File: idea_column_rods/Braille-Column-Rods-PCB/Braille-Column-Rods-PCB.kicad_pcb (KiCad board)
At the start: 2 copper layers, 76 x 95 mm, 64 parts, among them J1 Conn_01x06, J10 Screw_Terminal_01x02, J2 Conn_01x06, J3 Conn_01x06, J4 Conn_01x06, J9 Conn_01x02, M1 Stepper_Motor_bipolar, M2 Stepper_Motor_bipolar, M3 Stepper_Motor_bipolar, M4 Stepper_Motor_bipolar, SW1 SW_Push, SW2 SW_Push, U1 DRV8847SPWR, U2 DRV8847SPWR, U3 DRV8847SPWR, U4 DRV8847SPWR, U9 RP2040-Zero

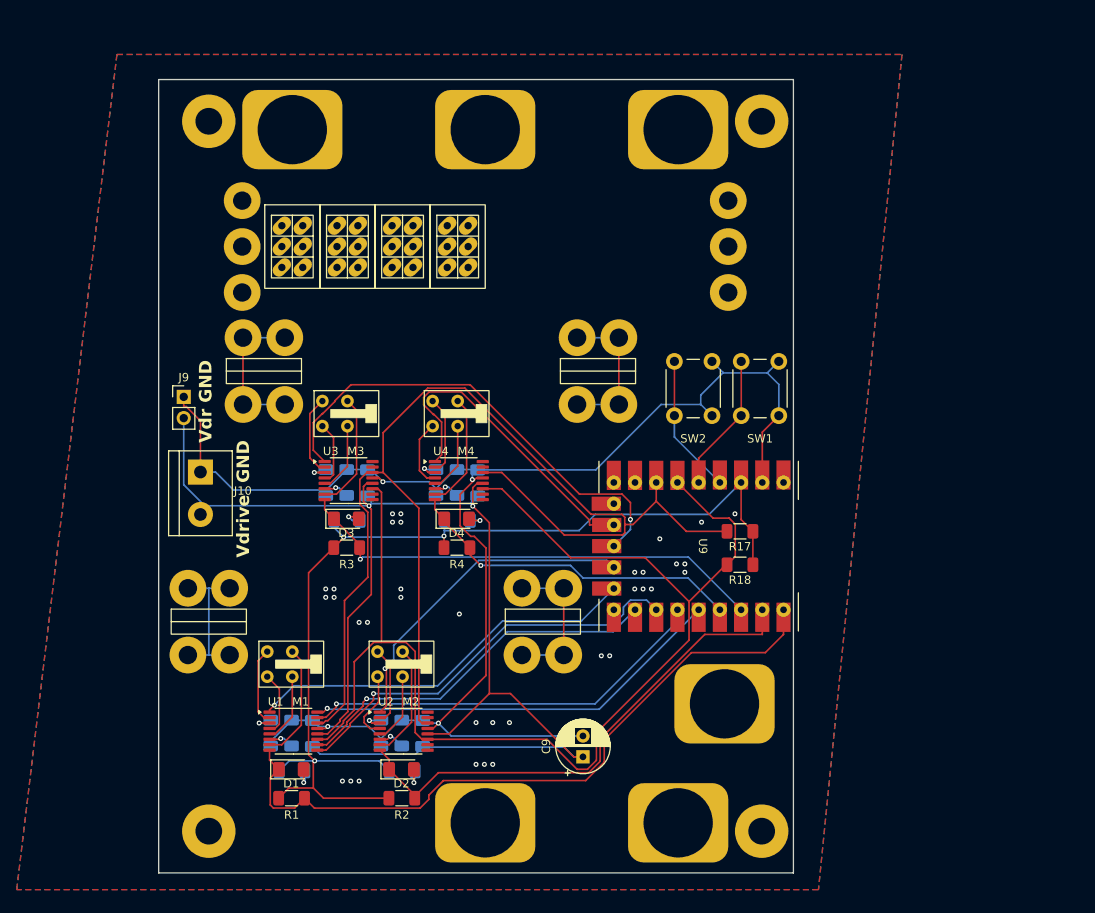
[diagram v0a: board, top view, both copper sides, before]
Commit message: Create PCB and CAD for Type 4 Rev 1 rod cams (#13)
* WIP: Rods PCB placement

* WIP: Place the housing and motor X

* WIP: Position everything

* WIP: Update tight placement of DC motor

* WIP: Layout and route the stepper driver

* WIP: Motor layout is good

* WIP: Manual routing and silkscreens

* Comments

* Big routing

* Clean up DRC (mostly footprints)

* Fix spacing issue on top

* Fix spacing issues on bottom

* Create render of 6mm motor, add to PCB

* WIP: Get cams good

* WIP: Reorder the cam bushing and hall sensor

* Finish and tag release

* Complete type 4 rev 1

* Create dc_motor_clamp cad
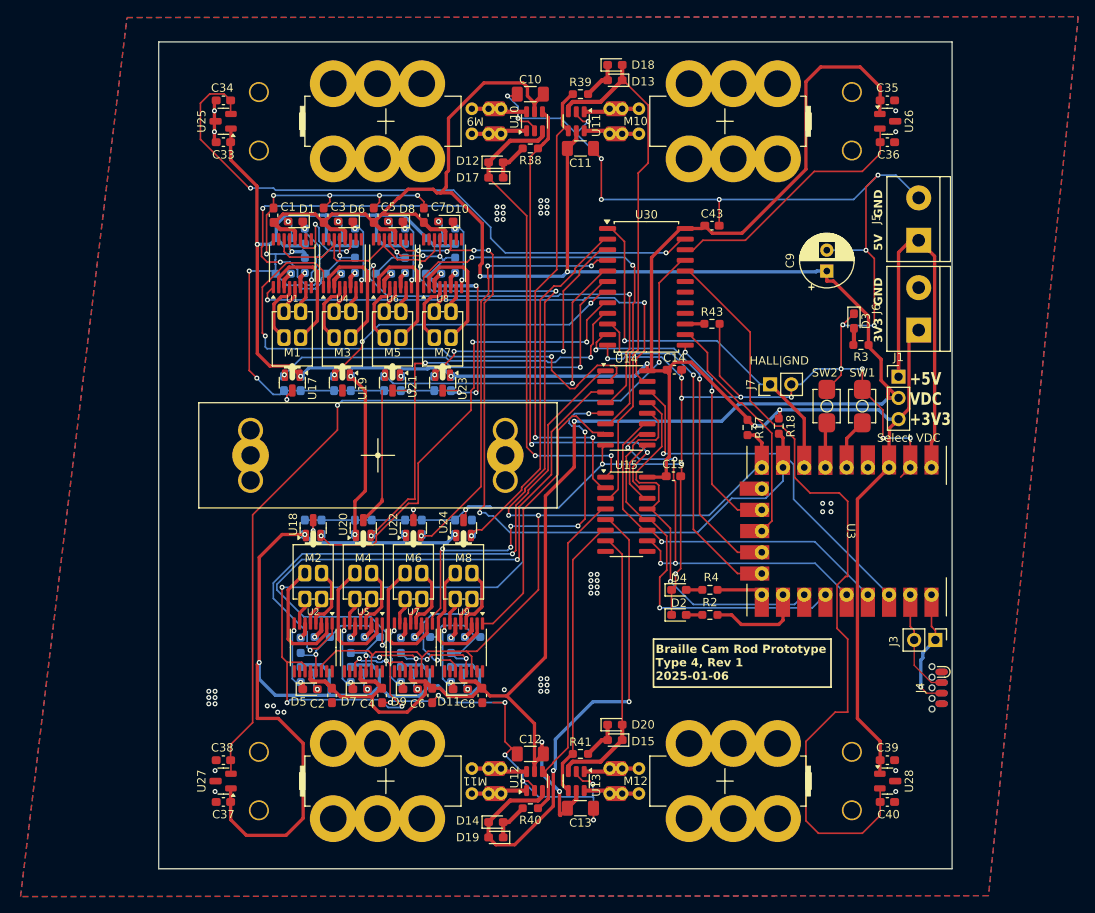
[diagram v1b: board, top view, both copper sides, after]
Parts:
- removed H10, H11, H12, H7, H8, H9: MountingHole_Pad, 00-lib-footprints:MountingHole_2.2mm_M2_Pad_NoSilk
- removed H13, H14, H15, H16: MountingHole_Pad, 00-lib-footprints:MountingHole_3.2mm_M3_Pad_NoSilk
- removed H17, H18, H19, H20: MountingHole_Pad, 00-lib-footprints:HorizMounting_4x_M2_and_M3_Middle
- removed H3, H4, H5, H6: MountingHole_Pad, 00-lib-footprints:MountingHole_8mm_Rect_NoSilk
- removed J10: Screw_Terminal_01x02, TerminalBlock:TerminalBlock_bornier-2_P5.08mm
- removed J2: Conn_01x06, 00-lib-footprints:Braille_Cell_Pogos_Solder_2.5mmIntra_6.6x10mmInter
- removed J9: Conn_01x02, Connector_PinHeader_2.54mm:PinHeader_1x02_P2.54mm_Vertical
- added C10: 10u, Capacitor_SMD:C_1206_3216Metric_Pad1.33x1.80mm_HandSolder, F.Cu at (128.5, 81.8)
- added C11: 10u, Capacitor_SMD:C_1206_3216Metric_Pad1.33x1.80mm_HandSolder, F.Cu at (134.5, 88.2)
- added C12: 10u, Capacitor_SMD:C_1206_3216Metric_Pad1.33x1.80mm_HandSolder, F.Cu at (128.5, 160.8)
- added C13: 10u, Capacitor_SMD:C_1206_3216Metric_Pad1.33x1.80mm_HandSolder, F.Cu at (134.5, 167.2)
- added C14: 100n, Capacitor_SMD:C_0603_1608Metric_Pad1.08x0.95mm_HandSolder, F.Cu at (145.8, 114.8)
- added C15: 100n, Capacitor_SMD:C_0603_1608Metric_Pad1.08x0.95mm_HandSolder, F.Cu at (145.6, 127.5)
- added C17: 100n, Capacitor_SMD:C_0603_1608Metric_Pad1.08x0.95mm_HandSolder, B.Cu at (101.0, 116.4)
- added C18: 100n, Capacitor_SMD:C_0603_1608Metric_Pad1.08x0.95mm_HandSolder, B.Cu at (101.5, 133.6)
- added C19: 100n, Capacitor_SMD:C_0603_1608Metric_Pad1.08x0.95mm_HandSolder, B.Cu at (107.0, 116.4)
- added C20: 100n, Capacitor_SMD:C_0603_1608Metric_Pad1.08x0.95mm_HandSolder, B.Cu at (107.5, 133.6)
- added C21: 100n, Capacitor_SMD:C_0603_1608Metric_Pad1.08x0.95mm_HandSolder, B.Cu at (113.0, 116.4)
- added C22: 100n, Capacitor_SMD:C_0603_1608Metric_Pad1.08x0.95mm_HandSolder, B.Cu at (113.5, 133.6)
- added C23: 100n, Capacitor_SMD:C_0603_1608Metric_Pad1.08x0.95mm_HandSolder, B.Cu at (119.0, 116.4)
- added C24: 100n, Capacitor_SMD:C_0603_1608Metric_Pad1.08x0.95mm_HandSolder, B.Cu at (119.5, 133.6)
- added C25: 4.7n, Capacitor_SMD:C_0603_1608Metric_Pad1.08x0.95mm_HandSolder, B.Cu at (99.0, 116.4)
- added C26: 4.7n, Capacitor_SMD:C_0603_1608Metric_Pad1.08x0.95mm_HandSolder, B.Cu at (103.5, 133.6)
- added C27: 4.7n, Capacitor_SMD:C_0603_1608Metric_Pad1.08x0.95mm_HandSolder, B.Cu at (105.0, 116.4)
- added C28: 4.7n, Capacitor_SMD:C_0603_1608Metric_Pad1.08x0.95mm_HandSolder, B.Cu at (109.5, 133.6)
- added C29: 4.7n, Capacitor_SMD:C_0603_1608Metric_Pad1.08x0.95mm_HandSolder, B.Cu at (111.0, 116.4)
- added C30: 4.7n, Capacitor_SMD:C_0603_1608Metric_Pad1.08x0.95mm_HandSolder, B.Cu at (115.5, 133.6)
- added C31: 4.7n, Capacitor_SMD:C_0603_1608Metric_Pad1.08x0.95mm_HandSolder, B.Cu at (117.0, 116.4)
- added C32: 4.7n, Capacitor_SMD:C_0603_1608Metric_Pad1.08x0.95mm_HandSolder, B.Cu at (121.5, 133.6)
- added C33: 100n, Capacitor_SMD:C_0603_1608Metric_Pad1.08x0.95mm_HandSolder, F.Cu at (91.8, 87.5)
- added C34: 4.7n, Capacitor_SMD:C_0603_1608Metric_Pad1.08x0.95mm_HandSolder, F.Cu at (91.8, 82.5)
- added C35: 100n, Capacitor_SMD:C_0603_1608Metric_Pad1.08x0.95mm_HandSolder, F.Cu at (171.2, 82.5)
- added C36: 4.7n, Capacitor_SMD:C_0603_1608Metric_Pad1.08x0.95mm_HandSolder, F.Cu at (171.2, 87.5)
- added C37: 100n, Capacitor_SMD:C_0603_1608Metric_Pad1.08x0.95mm_HandSolder, F.Cu at (91.8, 166.5)
- added C38: 4.7n, Capacitor_SMD:C_0603_1608Metric_Pad1.08x0.95mm_HandSolder, F.Cu at (91.8, 161.5)
- added C39: 100n, Capacitor_SMD:C_0603_1608Metric_Pad1.08x0.95mm_HandSolder, F.Cu at (171.2, 161.5)
- added C40: 4.7n, Capacitor_SMD:C_0603_1608Metric_Pad1.08x0.95mm_HandSolder, F.Cu at (171.2, 166.5)
- added C43: 100n, Capacitor_SMD:C_0603_1608Metric_Pad1.08x0.95mm_HandSolder, F.Cu at (150.2, 97.5)
- added C5: 100n, Capacitor_SMD:C_0603_1608Metric_Pad1.08x0.95mm_HandSolder, F.Cu at (109.8, 96.2)
- added C6: 100n, Capacitor_SMD:C_0603_1608Metric_Pad1.08x0.95mm_HandSolder, F.Cu at (116.8, 153.8)
- added C7: 100n, Capacitor_SMD:C_0603_1608Metric_Pad1.08x0.95mm_HandSolder, F.Cu at (115.8, 96.2)
- added C8: 100n, Capacitor_SMD:C_0603_1608Metric_Pad1.08x0.95mm_HandSolder, F.Cu at (122.8, 153.8)
- added D10: LED, LED_SMD:LED_0603_1608Metric_Pad1.05x0.95mm_HandSolder, F.Cu at (118.4, 97.0)
- added D11: LED, LED_SMD:LED_0603_1608Metric_Pad1.05x0.95mm_HandSolder, F.Cu at (120.1, 153.0)
- added D12: LED, LED_SMD:LED_0603_1608Metric_Pad1.05x0.95mm_HandSolder, F.Cu at (124.4, 89.9)
- added D13: LED, LED_SMD:LED_0603_1608Metric_Pad1.05x0.95mm_HandSolder, F.Cu at (138.6, 80.1)
- added D14: LED, LED_SMD:LED_0603_1608Metric_Pad1.05x0.95mm_HandSolder, F.Cu at (124.4, 168.9)
- added D15: LED, LED_SMD:LED_0603_1608Metric_Pad1.05x0.95mm_HandSolder, F.Cu at (138.6, 159.1)
- added D17: LED, LED_SMD:LED_0603_1608Metric_Pad1.05x0.95mm_HandSolder, F.Cu at (124.4, 91.8)
- added D18: LED, LED_SMD:LED_0603_1608Metric_Pad1.05x0.95mm_HandSolder, F.Cu at (138.6, 78.3)
- added D19: LED, LED_SMD:LED_0603_1608Metric_Pad1.05x0.95mm_HandSolder, F.Cu at (124.4, 170.8)
- added D20: LED, LED_SMD:LED_0603_1608Metric_Pad1.05x0.95mm_HandSolder, F.Cu at (138.6, 157.3)
- added D5: LED, LED_SMD:LED_0603_1608Metric_Pad1.05x0.95mm_HandSolder, F.Cu at (102.1, 153.0)
- added D6: LED, LED_SMD:LED_0603_1608Metric_Pad1.05x0.95mm_HandSolder, F.Cu at (106.4, 97.0)
- added D7: LED, LED_SMD:LED_0603_1608Metric_Pad1.05x0.95mm_HandSolder, F.Cu at (108.1, 153.0)
- added D8: LED, LED_SMD:LED_0603_1608Metric_Pad1.05x0.95mm_HandSolder, F.Cu at (112.4, 97.0)
- added D9: LED, LED_SMD:LED_0603_1608Metric_Pad1.05x0.95mm_HandSolder, F.Cu at (114.1, 153.0)
- added J5: Screw_Terminal_01x02, TerminalBlock:TerminalBlock_bornier-2_P5.08mm, F.Cu at (175.0, 99.2)
- added J6: Screw_Terminal_01x02, TerminalBlock:TerminalBlock_bornier-2_P5.08mm, F.Cu at (175.0, 110.0)
- added J7: Conn_01x02, Connector_PinHeader_2.54mm:PinHeader_1x02_P2.54mm_Vertical, F.Cu at (157.2, 116.5)
- added M10: Motor_DC_With_MP, 00-lib-footprints:DC_Motor_6mm_OD_with_3_Stage_Gearbox, F.Cu at (162.6, 85.0)
- added M11: Motor_DC_With_MP, 00-lib-footprints:DC_Motor_6mm_OD_with_3_Stage_Gearbox, F.Cu at (100.4, 164.0)
- added M12: Motor_DC_With_MP, 00-lib-footprints:DC_Motor_6mm_OD_with_3_Stage_Gearbox, F.Cu at (162.6, 164.0)
- added M5: Stepper_Motor_bipolar, 00-lib-footprints:MicroStepper_4.7_OD, F.Cu at (112.0, 114.7)
- added M6: Stepper_Motor_bipolar, 00-lib-footprints:MicroStepper_4.7_OD, F.Cu at (114.5, 135.3)
- added M7: Stepper_Motor_bipolar, 00-lib-footprints:MicroStepper_4.7_OD, F.Cu at (118.0, 114.7)
- added M8: Stepper_Motor_bipolar, 00-lib-footprints:MicroStepper_4.7_OD, F.Cu at (120.5, 135.3)
- added M9: Motor_DC_With_MP, 00-lib-footprints:DC_Motor_6mm_OD_with_3_Stage_Gearbox, F.Cu at (100.4, 85.0)
- added R13: 2k1, Resistor_SMD:R_0603_1608Metric_Pad0.98x0.95mm_HandSolder, B.Cu at (105.0, 99.0)
- added R14: 330m, Resistor_SMD:R_0603_1608Metric_Pad0.98x0.95mm_HandSolder, B.Cu at (107.5, 102.2)
- added R15: 330m, Resistor_SMD:R_0603_1608Metric_Pad0.98x0.95mm_HandSolder, B.Cu at (104.9, 103.2)
- added R16: 5k1, Resistor_SMD:R_0603_1608Metric_Pad0.98x0.95mm_HandSolder, B.Cu at (107.0, 151.2)
- added R23: 2k1, Resistor_SMD:R_0603_1608Metric_Pad0.98x0.95mm_HandSolder, B.Cu at (111.0, 99.0)
- added R24: 330m, Resistor_SMD:R_0603_1608Metric_Pad0.98x0.95mm_HandSolder, B.Cu at (113.5, 102.2)
- added R25: 330m, Resistor_SMD:R_0603_1608Metric_Pad0.98x0.95mm_HandSolder, B.Cu at (110.9, 103.2)
- added R26: 5k1, Resistor_SMD:R_0603_1608Metric_Pad0.98x0.95mm_HandSolder, B.Cu at (113.0, 151.2)
- added R31: 2k1, Resistor_SMD:R_0603_1608Metric_Pad0.98x0.95mm_HandSolder, B.Cu at (117.0, 99.0)
- added R32: 330m, Resistor_SMD:R_0603_1608Metric_Pad0.98x0.95mm_HandSolder, B.Cu at (119.5, 102.2)
- added R33: 330m, Resistor_SMD:R_0603_1608Metric_Pad0.98x0.95mm_HandSolder, B.Cu at (116.9, 103.2)
- added R34: 5k1, Resistor_SMD:R_0603_1608Metric_Pad0.98x0.95mm_HandSolder, B.Cu at (119.0, 151.2)
- added R35: 2k1, Resistor_SMD:R_0603_1608Metric_Pad0.98x0.95mm_HandSolder, B.Cu at (121.5, 151.0)
- added R36: 330m, Resistor_SMD:R_0603_1608Metric_Pad0.98x0.95mm_HandSolder, B.Cu at (119.0, 147.8)
- added R37: 330m, Resistor_SMD:R_0603_1608Metric_Pad0.98x0.95mm_HandSolder, B.Cu at (121.6, 146.8)
- added R38: 5k1, Resistor_SMD:R_0603_1608Metric_Pad0.98x0.95mm_HandSolder, F.Cu at (128.5, 88.2)
- added R39: 5k1, Resistor_SMD:R_0603_1608Metric_Pad0.98x0.95mm_HandSolder, F.Cu at (134.5, 81.8)
- added R40: 5k1, Resistor_SMD:R_0603_1608Metric_Pad0.98x0.95mm_HandSolder, F.Cu at (128.5, 167.2)
- added R41: 5k1, Resistor_SMD:R_0603_1608Metric_Pad0.98x0.95mm_HandSolder, F.Cu at (134.5, 160.8)
- added R43: 5k1, Resistor_SMD:R_0603_1608Metric_Pad0.98x0.95mm_HandSolder, F.Cu at (150.2, 109.2)
- added R5: 2k1, Resistor_SMD:R_0603_1608Metric_Pad0.98x0.95mm_HandSolder, B.Cu at (99.0, 99.0)
- added R6: 330m, Resistor_SMD:R_0603_1608Metric_Pad0.98x0.95mm_HandSolder, B.Cu at (101.5, 102.2)
- added R7: 330m, Resistor_SMD:R_0603_1608Metric_Pad0.98x0.95mm_HandSolder, B.Cu at (98.9, 103.2)
- added R8: 5k1, Resistor_SMD:R_0603_1608Metric_Pad0.98x0.95mm_HandSolder, B.Cu at (101.0, 151.2)
- added U10: AD116, Package_TO_SOT_SMD:SOT-23-6, F.Cu at (129.0, 85.0)
- added U11: AD116, Package_TO_SOT_SMD:SOT-23-6, F.Cu at (134.0, 85.0)
- added U12: AD116, Package_TO_SOT_SMD:SOT-23-6, F.Cu at (129.0, 164.0)
- added U13: AD116, Package_TO_SOT_SMD:SOT-23-6, F.Cu at (134.0, 164.0)
- added U14: 74HC595, Package_SO:SOP-16_3.9x9.9mm_P1.27mm, F.Cu at (140.0, 119.3)
- added U15: 74HC595, Package_SO:SOP-16_3.9x9.9mm_P1.27mm, F.Cu at (140.0, 132.1)
- added U17: MT910xET, 00-lib-footprints:SOT-23-Hall, F.Cu at (100.0, 116.3)
- added U18: MT910xET, 00-lib-footprints:SOT-23-Hall, F.Cu at (102.5, 133.7)
- added U19: MT910xET, 00-lib-footprints:SOT-23-Hall, F.Cu at (106.0, 116.3)
- added U20: MT910xET, 00-lib-footprints:SOT-23-Hall, F.Cu at (108.5, 133.7)
- added U21: MT910xET, 00-lib-footprints:SOT-23-Hall, F.Cu at (112.0, 116.3)
- added U22: MT910xET, 00-lib-footprints:SOT-23-Hall, F.Cu at (114.5, 133.7)
- added U23: MT910xET, 00-lib-footprints:SOT-23-Hall, F.Cu at (118.0, 116.3)
- added U24: MT910xET, 00-lib-footprints:SOT-23-Hall, F.Cu at (120.5, 133.7)
- added U25: MT910xET, 00-lib-footprints:SOT-23-Hall, F.Cu at (91.8, 85.0)
- added U26: MT910xET, 00-lib-footprints:SOT-23-Hall, F.Cu at (171.2, 85.0)
- added U27: MT910xET, 00-lib-footprints:SOT-23-Hall, F.Cu at (91.8, 164.0)
- added U28: MT910xET, 00-lib-footprints:SOT-23-Hall, F.Cu at (171.2, 164.0)
- added U30: CD74HC4067M, Package_SO:SOIC-24W_7.5x15.4mm_P1.27mm, F.Cu at (142.4, 104.8)
- added U5: DRV8847SPWR, Package_SO:TSSOP-16_4.4x5mm_P0.65mm, F.Cu at (108.5, 148.0)
- added U6: DRV8847SPWR, Package_SO:TSSOP-16_4.4x5mm_P0.65mm, F.Cu at (112.0, 102.0)
- added U7: DRV8847SPWR, Package_SO:TSSOP-16_4.4x5mm_P0.65mm, F.Cu at (114.5, 148.0)
- added U8: DRV8847SPWR, Package_SO:TSSOP-16_4.4x5mm_P0.65mm, F.Cu at (118.0, 102.0)
- C1, C2, C3, C4: footprint Capacitor_SMD:C_1206_3216Metric_Pad1.33x1.80mm_HandSolder -> Capacitor_SMD:C_0603_1608Metric_Pad1.08x0.95mm_HandSolder; moved to F.Cu
- D1, D2, D3, D4: footprint LED_SMD:LED_1206_3216Metric_Pad1.42x1.75mm_HandSolder -> LED_SMD:LED_0603_1608Metric_Pad1.05x0.95mm_HandSolder
- H1, H2: footprint 00-lib-footprints:MountingHole_8mm_Rect_NoSilk -> 00-lib-footprints:Braille_Block_MountingHoles_M2_3x
- J1: value Conn_01x06 -> Conn_01x03; footprint 00-lib-footprints:Braille_Cell_Pogos_Solder_2.5mmIntra_6.6x10mmInter -> Connector_PinHeader_2.54mm:PinHeader_1x03_P2.54mm_Vertical
- J3: value Conn_01x06 -> Conn_01x02; footprint 00-lib-footprints:Braille_Cell_Pogos_Solder_2.5mmIntra_6.6x10mmInter -> Connector_PinHeader_2.54mm:PinHeader_1x02_P2.54mm_Vertical
- J4: value Conn_01x06 -> Conn_01x08; footprint 00-lib-footprints:Braille_Cell_Pogos_Solder_2.5mmIntra_6.6x10mmInter -> 00-lib-footprints:SOICbite_clipProgSmall
- M1, M2, M3, M4: footprint 00-lib-footprints:MicroStepper_8mm-2mmGear -> 00-lib-footprints:MicroStepper_4.7_OD
- R1: footprint Resistor_SMD:R_1206_3216Metric_Pad1.30x1.75mm_HandSolder -> Resistor_SMD:R_0603_1608Metric_Pad0.98x0.95mm_HandSolder; moved to B.Cu
- R10, R11: value 2k1 -> 330m; footprint Resistor_SMD:R_1206_3216Metric_Pad1.30x1.75mm_HandSolder -> Resistor_SMD:R_0603_1608Metric_Pad0.98x0.95mm_HandSolder
- R12: value 2k1 -> 5k1; footprint Resistor_SMD:R_1206_3216Metric_Pad1.30x1.75mm_HandSolder -> Resistor_SMD:R_0603_1608Metric_Pad0.98x0.95mm_HandSolder
- R17, R18, R2, R20, R21, R28, R29, R3, R4, R9: footprint Resistor_SMD:R_1206_3216Metric_Pad1.30x1.75mm_HandSolder -> Resistor_SMD:R_0603_1608Metric_Pad0.98x0.95mm_HandSolder
- R19, R27: value 330m -> 2k1; footprint Resistor_SMD:R_1206_3216Metric_Pad1.30x1.75mm_HandSolder -> Resistor_SMD:R_0603_1608Metric_Pad0.98x0.95mm_HandSolder
- R22, R30: value 330m -> 5k1; footprint Resistor_SMD:R_1206_3216Metric_Pad1.30x1.75mm_HandSolder -> Resistor_SMD:R_0603_1608Metric_Pad0.98x0.95mm_HandSolder
- SW1, SW2: footprint Button_Switch_THT:SW_PUSH_6mm -> 00-lib-footprints:PushButtonSMD_2.93x3.9
- U3: value DRV8847SPWR -> RP2040-Zero; footprint Package_SO:TSSOP-16_4.4x5mm_P0.65mm -> 00-lib-footprints:RP2040 Zero
- U9: value RP2040-Zero -> DRV8847SPWR; footprint 00-lib-footprints:RP2040 Zero -> Package_SO:TSSOP-16_4.4x5mm_P0.65mm
- moved J3 84.7 mm to (177.0, 147.1), turned to -90 degrees
- moved J4 79.0 mm to (178.5, 152.8), turned to 90 degrees
- moved J1 74.2 mm to (172.6, 115.6)
- moved R1 67.3 mm to (101.5, 98.8), turned to 90 degrees
- moved R3 66.2 mm to (168.1, 111.8), turned to 180 degrees
- moved D1 65.6 mm to (100.4, 97.0), turned to 180 degrees
- moved D3 65.2 mm to (167.2, 108.9), turned to -90 degrees
- moved C9 65.1 mm to (164.0, 102.9)
- moved C1 62.2 mm to (97.8, 96.2)
- moved U1 56.0 mm to (100.0, 102.0), turned to 90 degrees
- moved H1 48.1 mm to (95.0, 125.0)
- moved U3 47.0 mm to (153.5, 123.9), turned to -90 degrees
- moved H2 44.1 mm to (125.5, 125.0)
- moved R2 42.9 mm to (150.0, 144.1), turned to 180 degrees
- moved D2 38.0 mm to (146.3, 144.1)
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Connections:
- C1 pad 1: Vdrive -> VDC
- C2 pad 1: Vdrive -> VDC
- C3 pad 1: Vdrive -> VDC
- C4 pad 1: Vdrive -> VDC
- C9 pad 1: Vdrive -> VDC
- D1 pad 1: /Braille_Cell/~{FAULT} -> /Motor_Control/Braille_Cell_Column/~{FAULT}
- D2 pad 1: /Braille_Cell1/~{FAULT} -> GND
- D3 pad 1: /Braille_Cell2/~{FAULT} -> GND
- D4 pad 1: /Braille_Cell3/~{FAULT} -> GND
- J1 pad 1: unconnected-(J1-Pin_1-Pad1) -> +5V
- J1 pad 2: unconnected-(J1-Pin_2-Pad2) -> VDC
- J1 pad 3: unconnected-(J1-Pin_3-Pad3) -> +3V3
- J3 pad 1: unconnected-(J3-Pin_1-Pad1) -> /Microcontroller/UART0_TX
- J3 pad 2: unconnected-(J3-Pin_2-Pad2) -> /Microcontroller/UART0_RX
- J4 pad 2: unconnected-(J4-Pin_2-Pad2) -> /Microcontroller/UART0_RX
- J4 pad 3: unconnected-(J4-Pin_3-Pad3) -> /Microcontroller/UART0_TX
- J4 pad 4: unconnected-(J4-Pin_4-Pad4) -> GND
- M3 pad 1: Net-(U3-OUT1) -> Net-(U4-OUT1)
- M3 pad 3: Net-(U3-OUT3) -> Net-(U4-OUT3)
- M3 pad 4: Net-(U3-OUT4) -> Net-(U4-OUT4)
- M4 pad 1: Net-(U4-OUT1) -> Net-(U5-OUT1)
- M4 pad 3: Net-(U4-OUT3) -> Net-(U5-OUT3)
- M4 pad 4: Net-(U4-OUT4) -> Net-(U5-OUT4)
- R1 pad 2: /Braille_Cell/~{FAULT} -> /Motor_Control/Braille_Cell_Column/~{FAULT}
- R10 pad 1: +3V3 -> Net-(U2-ISEN34)
- R10 pad 2: Net-(D2-A) -> GND
- R11 pad 1: +3V3 -> Net-(U2-ISEN12)
- R11 pad 2: Net-(D3-A) -> GND
- R12 pad 2: Net-(D4-A) -> /Motor_Control/Braille_Cell_Column2/~{FAULT}
- R19 pad 1: Net-(U1-ISEN34) -> +3V3
- R19 pad 2: GND -> Net-(D7-A)
- R2 pad 1: +3V3 -> /Microcontroller/GP_LED_0
- R2 pad 2: /Braille_Cell1/~{FAULT} -> Net-(D2-A)
- R20 pad 1: Net-(U2-ISEN34) -> Net-(U5-ISEN34)
- R21 pad 1: Net-(U3-ISEN34) -> Net-(U5-ISEN12)
- R22 pad 1: Net-(U4-ISEN34) -> +3V3
- R22 pad 2: GND -> /Motor_Control/Braille_Cell_Column4/~{FAULT}
- R27 pad 1: Net-(U1-ISEN12) -> +3V3
- R27 pad 2: GND -> Net-(D9-A)
- R28 pad 1: Net-(U2-ISEN12) -> Net-(U7-ISEN34)
- R29 pad 1: Net-(U3-ISEN12) -> Net-(U7-ISEN12)
- R3 pad 1: +3V3 -> VDC
- R3 pad 2: /Braille_Cell2/~{FAULT} -> Net-(D3-A)
- R30 pad 1: Net-(U4-ISEN12) -> +3V3
- R30 pad 2: GND -> /Motor_Control/Braille_Cell_Column6/~{FAULT}
- R4 pad 1: +3V3 -> /Microcontroller/GP_LED_1
- R4 pad 2: /Braille_Cell3/~{FAULT} -> Net-(D4-A)
- R9 pad 2: Net-(D1-A) -> Net-(D5-A)
- SW1 pad 2: Net-(U9-GP28) -> /Microcontroller/SW_1
- SW2 pad 2: Net-(U9-GP29) -> /Microcontroller/SW_2
- U1 pad 1: /Braille_Cell/~{SLEEP} -> /Motor_Control/Braille_Cell_Column/~{SLEEP}
- U1 pad 10: /Braille_Cell/IN4 -> unconnected-(U1-IN4-Pad10)
- U1 pad 12: Vdrive -> VDC
- U1 pad 15: /Braille_Cell/IN2 -> unconnected-(U1-IN2-Pad15)
- U1 pad 16: /Braille_Cell/IN1 -> unconnected-(U1-IN1-Pad16)
- U1 pad 8: /Braille_Cell/~{FAULT} -> /Motor_Control/Braille_Cell_Column/~{FAULT}
- U1 pad 9: /Braille_Cell/IN3 -> unconnected-(U1-IN3-Pad9)
- U2 pad 1: /Braille_Cell1/~{SLEEP} -> /Motor_Control/Braille_Cell_Column1/~{SLEEP}
- U2 pad 10: /Braille_Cell1/IN4 -> unconnected-(U2-IN4-Pad10)
- U2 pad 12: Vdrive -> VDC
- U2 pad 15: /Braille_Cell1/IN2 -> unconnected-(U2-IN2-Pad15)
- U2 pad 16: /Braille_Cell1/IN1 -> unconnected-(U2-IN1-Pad16)
- U2 pad 8: /Braille_Cell1/~{FAULT} -> /Motor_Control/Braille_Cell_Column1/~{FAULT}
- U2 pad 9: /Braille_Cell1/IN3 -> unconnected-(U2-IN3-Pad9)
- U3 pad 1: /Braille_Cell2/~{SLEEP} -> +5V
- U3 pad 10: /Braille_Cell2/IN4 -> /Microcontroller/UART0_TX
- U3 pad 11: I2C_SCL -> /Microcontroller/UART0_RX
- U3 pad 12: Vdrive -> /Microcontroller/SHIFT_SER_IN
- U3 pad 13: GND -> /Microcontroller/SHIFT_SRCK
- U3 pad 14: I2C_SDA -> /Microcontroller/~{SHIFT_SRCLR}
- U3 pad 15: /Braille_Cell2/IN2 -> /Microcontroller/SHIFT_RCLK
- U3 pad 16: /Braille_Cell2/IN1 -> /Microcontroller/~{SHIFT_OE}
- U3 pad 2: Net-(U3-OUT1) -> GND
- U3 pad 3: Net-(U3-ISEN12) -> +3V3
- U3 pad 4: Net-(M3--) -> unconnected-(U3-GP29-Pad4)
- U3 pad 5: Net-(U3-OUT4) -> /Microcontroller/SW_1
- U3 pad 6: Net-(U3-ISEN34) -> /Microcontroller/SW_2
- U3 pad 7: Net-(U3-OUT3) -> /Microcontroller/HALL_ANALOG
- U3 pad 8: /Braille_Cell2/~{FAULT} -> I2C_SCL
- U3 pad 9: /Braille_Cell2/IN3 -> I2C_SDA
- U4 pad 1: /Braille_Cell3/~{SLEEP} -> /Motor_Control/Braille_Cell_Column2/~{SLEEP}
- U4 pad 10: /Braille_Cell3/IN4 -> unconnected-(U4-IN4-Pad10)
- U4 pad 12: Vdrive -> VDC
- U4 pad 15: /Braille_Cell3/IN2 -> unconnected-(U4-IN2-Pad15)
- U4 pad 16: /Braille_Cell3/IN1 -> unconnected-(U4-IN1-Pad16)
- U4 pad 4: Net-(M4--) -> Net-(M3--)
- U4 pad 8: /Braille_Cell3/~{FAULT} -> /Motor_Control/Braille_Cell_Column2/~{FAULT}
- U4 pad 9: /Braille_Cell3/IN3 -> unconnected-(U4-IN3-Pad9)
- U9 pad 1: +5V -> /Motor_Control/Braille_Cell_Column7/~{SLEEP}
- U9 pad 10: /Braille_Cell/~{FAULT} -> unconnected-(U9-IN4-Pad10)
- U9 pad 11: /Braille_Cell1/~{FAULT} -> I2C_SCL
- U9 pad 12: /Braille_Cell2/~{FAULT} -> VDC
- U9 pad 13: /Braille_Cell3/~{FAULT} -> GND
- U9 pad 14: /Braille_Cell/IN1 -> I2C_SDA
- U9 pad 15: /Braille_Cell/IN2 -> unconnected-(U9-IN2-Pad15)
- U9 pad 16: /Braille_Cell/IN3 -> unconnected-(U9-IN1-Pad16)
- U9 pad 2: GND -> Net-(U9-OUT1)
- U9 pad 3: +3V3 -> Net-(U9-ISEN12)
- U9 pad 4: Net-(U9-GP29) -> Net-(M8--)
- U9 pad 5: Net-(U9-GP28) -> Net-(U9-OUT4)
- U9 pad 6: I2C_SCL -> Net-(U9-ISEN34)
- U9 pad 7: I2C_SDA -> Net-(U9-OUT3)
- U9 pad 8: unconnected-(U9-GP15-Pad8)_1 -> /Motor_Control/Braille_Cell_Column7/~{FAULT}
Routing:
- net GND: track 192.0 -> 530.2 mm, vias 39 -> 104
- net +3V3: track 127.6 -> 448.9 mm, vias 3 -> 13
- net VDC: track 0.00 -> 314.4 mm, vias 0 -> 5
- net Vdrive: track 166.6 -> 0.00 mm, vias 2 -> 0
- net /Motor_Control/HALL_10: track 0.00 -> 103.8 mm, vias 0 -> 2
- net I2C_SCL: track 148.8 -> 251.8 mm, vias 0 -> 15
- net /Motor_Control/HALL_11: track 0.00 -> 94.4 mm
- net /Braille_Cell/~{FAULT}: track 83.4 -> 0.00 mm
- net /Motor_Control/Braille_Cell_Column3/~{SLEEP}: track 0.00 -> 75.7 mm, vias 0 -> 2
- net /Motor_Control/HALL_8: track 0.00 -> 75.5 mm, vias 0 -> 2
- net /Motor_Control/Braille_Cell_Column1/~{SLEEP}: track 0.00 -> 71.4 mm, vias 0 -> 2
- net /Motor_Control/Braille_Cell_Column2/~{SLEEP}: track 0.00 -> 67.0 mm, vias 0 -> 2
- net /Motor_Control/Corner_DC_Motor1/IN_B: track 0.00 -> 64.0 mm
- net /Motor_Control/Corner_DC_Motor/IN_A: track 0.00 -> 62.6 mm, vias 0 -> 2
- net /Motor_Control/Corner_DC_Motor2/IN_B: track 0.00 -> 62.3 mm, vias 0 -> 2
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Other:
- board size 76 x 95 mm -> 95 x 99 mm
- board text added: "* Cell Housing: * Mounting hole spacing (X) = 30.5mm * Center = (110.25mm, 125mm) * Rods Dimensions: * Back Side X Vals: [98.75, 104.75, 110.75, 116.75] * Front Side X Vals: [103.75, 109.75, 115.75, 121.75] * magnet_coord_y: 8.7 * motor_shaft_gripper_max_y: 10.3"
- board text added: "+5V VDC +3V3"
- board text added: "3V3 GND"
- board text added: "5V GND"
- board text added: "Braille Cam Rod Prototype Type 4, Rev 1 2025-01-06"
- board text added: "HALL|GND"
- board text added: "Select VDC"
- board text removed: "6.6mm Inter-Cell 2.5mm Intra-Cell M2, M3, and 8mm"
- board text removed: "Braille Display (Pogo + Solenoid) 2024-10-10"
- board text removed: "Vdr GND"
- board text removed: "Vdrive GND"
